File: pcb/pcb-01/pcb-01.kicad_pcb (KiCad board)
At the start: 4 copper layers, 78 x 58 mm, 170 parts, among them J1 POWER, J2 MOTOR, J3 HALL, J4 TEMP, J5 I2C, J6 USB-C, J7 PROGRAM, J8 DNP 2x5 1.27mm, Q1 DMP6023LE-13, Q2 2N7002K, Q3 2N7002, SW1 SW_Push, SW2 SW_Push, SW3 SW_Push, U1 MCF8316DVRGFR, U10 SN74LVC1G17DCKR, U11 SN74LVC1G17DCKR, U12 TPD2EUSB30, U2 ESP32-C6-MINI-1, U3 TPSM365R6V3RDNR, U4 TPS7A1601DGN, U5 SN74LVC1G74DCTR, U6 SN74LVC1G74DCTR, U7 TPS3435CAKAGDD, U8 LM2907M-14, U9 TLV1701DBV

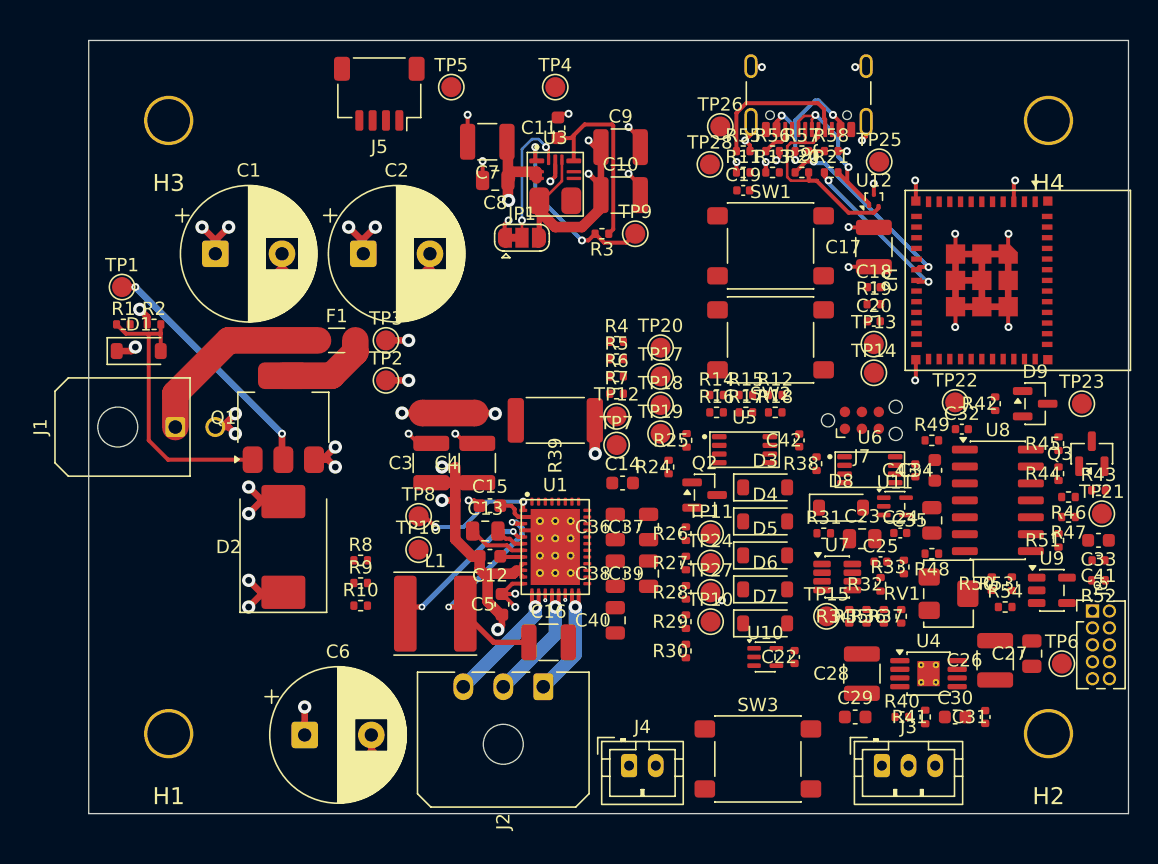
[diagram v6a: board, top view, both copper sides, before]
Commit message: pcb: all point-to-point routing done — digital fan-out + tach analog + J8
Digital fan-out (I2C/J5, SPEED/DIR/BRAKE straps, FG/NFAULT/ALARM, buttons/
J7/UART, PGOOD, watchdog web, DRVOFF, TEMP_SENSE), the full tach + safety
analog block (LDO feed, +12V star, Hall front-end, LM2907, comparator,
latch web), J8 debug legs, and the old RAW24 gap — every functional net
routed, validated at the DRC baseline per chunk. Board min via 0.4/0.2 now
actually in Board Setup. Remaining: J8 VM24/PGND taps, AGND/3V3 fills +
stitching, J8.3 starved thermal, waiver re-triage, silk sweep.

Five new /pcb quirks (unfill-storm, duplicate button pads, micro vias,
buried duplicate stubs, board-setup constraints not landing); routing
notes extended in electrical.md; STATE.md rewritten.
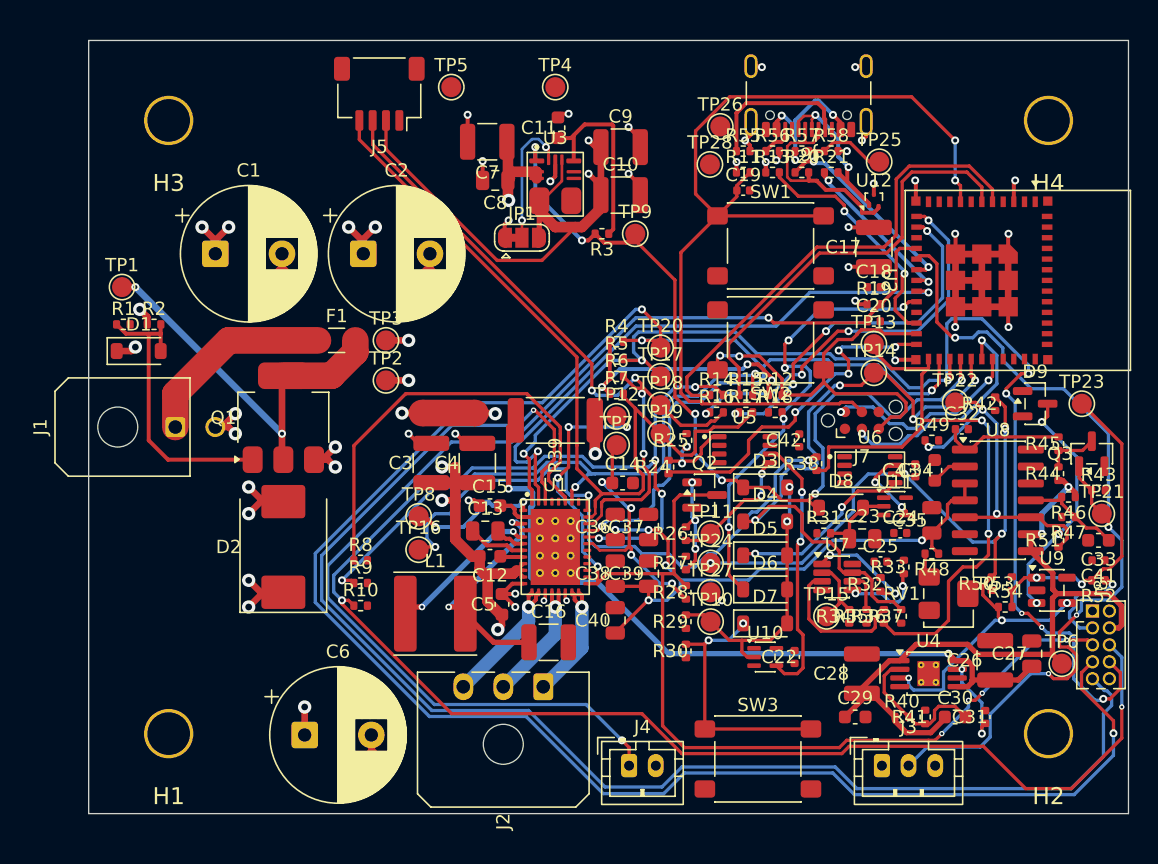
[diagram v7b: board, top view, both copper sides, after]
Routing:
- net FG: track 0.00 -> 169.2 mm, vias 0 -> 5
- net SPEED: track 0.00 -> 126.7 mm, vias 0 -> 6
- net SOX: track 0.00 -> 105.6 mm, vias 0 -> 1
- net NFAULT: track 0.00 -> 95.4 mm, vias 0 -> 8
- net TEMP_SENSE: track 0.00 -> 87.2 mm, vias 0 -> 2
- net DRVOFF: track 0.00 -> 83.9 mm, vias 0 -> 8
- net ESP_EN: track 0.00 -> 74.7 mm, vias 0 -> 2
- net HALL_TACH: track 0.00 -> 68.0 mm, vias 0 -> 4
- net OVERSPEED_N: track 0.00 -> 63.9 mm, vias 0 -> 7
- net SCL: track 0.00 -> 61.8 mm
- net /SCH-06 Hall Tach/TACH_LDO_IN: track 0.00 -> 57.0 mm, vias 0 -> 2
- net SDA: track 0.00 -> 56.1 mm, vias 0 -> 4
- net +12V_TACH: track 0.00 -> 52.6 mm, vias 0 -> 2
- net PGOOD: track 14.3 -> 66.2 mm, vias 2 -> 6
- net 3V3: track 26.0 -> 75.1 mm, vias 6 -> 11
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
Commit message: pcb: routing complete — B.Cu fill, full stitch sweep, zero unconnected
J8 VM24/PGND plane taps (PGND reuses TP27's via), agnd-bcu B.Cu zone,
87 AGND + 29 3V3 stitch items closed via rules-based sweep, antenna
keepout trimmed off U2's ground column (121 -> 122.4), .kicad_dru
mounting-hole rule scoped to pads, starved thermals fixed with solid
zone connections. Final DRC: unconnected 0, all residuals waived in
placement/waivers.md. Remaining: silk sweep + fab outputs.
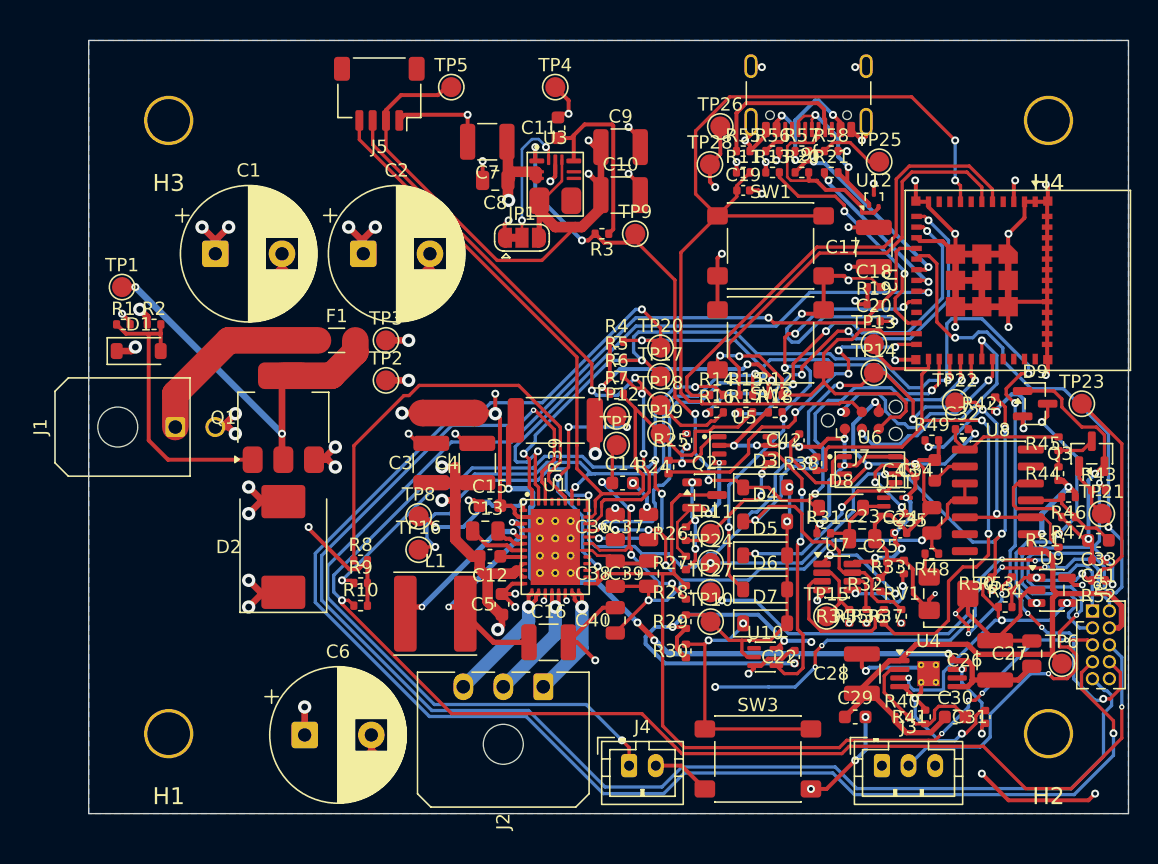
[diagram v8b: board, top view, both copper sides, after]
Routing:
- net AGND: track 57.5 -> 329.4 mm, vias 22 -> 60
- net 3V3: track 75.1 -> 179.7 mm, vias 11 -> 35
- net VM24: track 57.5 -> 94.8 mm, vias 17 -> 22
- net PGND: track 36.6 -> 73.6 mm, vias 19 -> 21
- net HALL_TACH: track 68.0 -> 80.5 mm
- net /SCH-06 Hall Tach/TLV_INN: track 18.0 -> 19.9 mm
- net UART_TX: track 15.4 -> 16.6 mm
- net VTACH: track 26.1 -> 25.1 mm
- net FG: track 169.2 -> 170.0 mm
- net +12V_TACH: track 52.6 -> 53.2 mm
- net /SCH-04 ESP32-C6 Supervisor/ESP_SCL: track 26.8 -> 27.4 mm
- net /SCH-03 MCF Power Stage/MCF_BRAKE: track 33.2 -> 33.7 mm
- net /SCH-06 Hall Tach/TACH_LDO_IN: vias 2 -> 4
- added copper zone on B.Cu, net AGND
